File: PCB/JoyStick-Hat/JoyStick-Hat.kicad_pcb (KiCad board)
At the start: 4 copper layers, 65 x 120 mm, 114 parts, among them J1 20021121-00010C4LF, J10 Conn_02x06_Odd_Even, J14 Conn_01x03_Pin, J15 Conn_01x03_Pin, J2 BU2032SM-JJ-GTR, J3 Conn_02x05_Odd_Even, J4 Conn_02x04_Odd_Even, J5 8P8C_LED_Shielded, J6 1757242, J7 Raspberry_Pi_2_3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

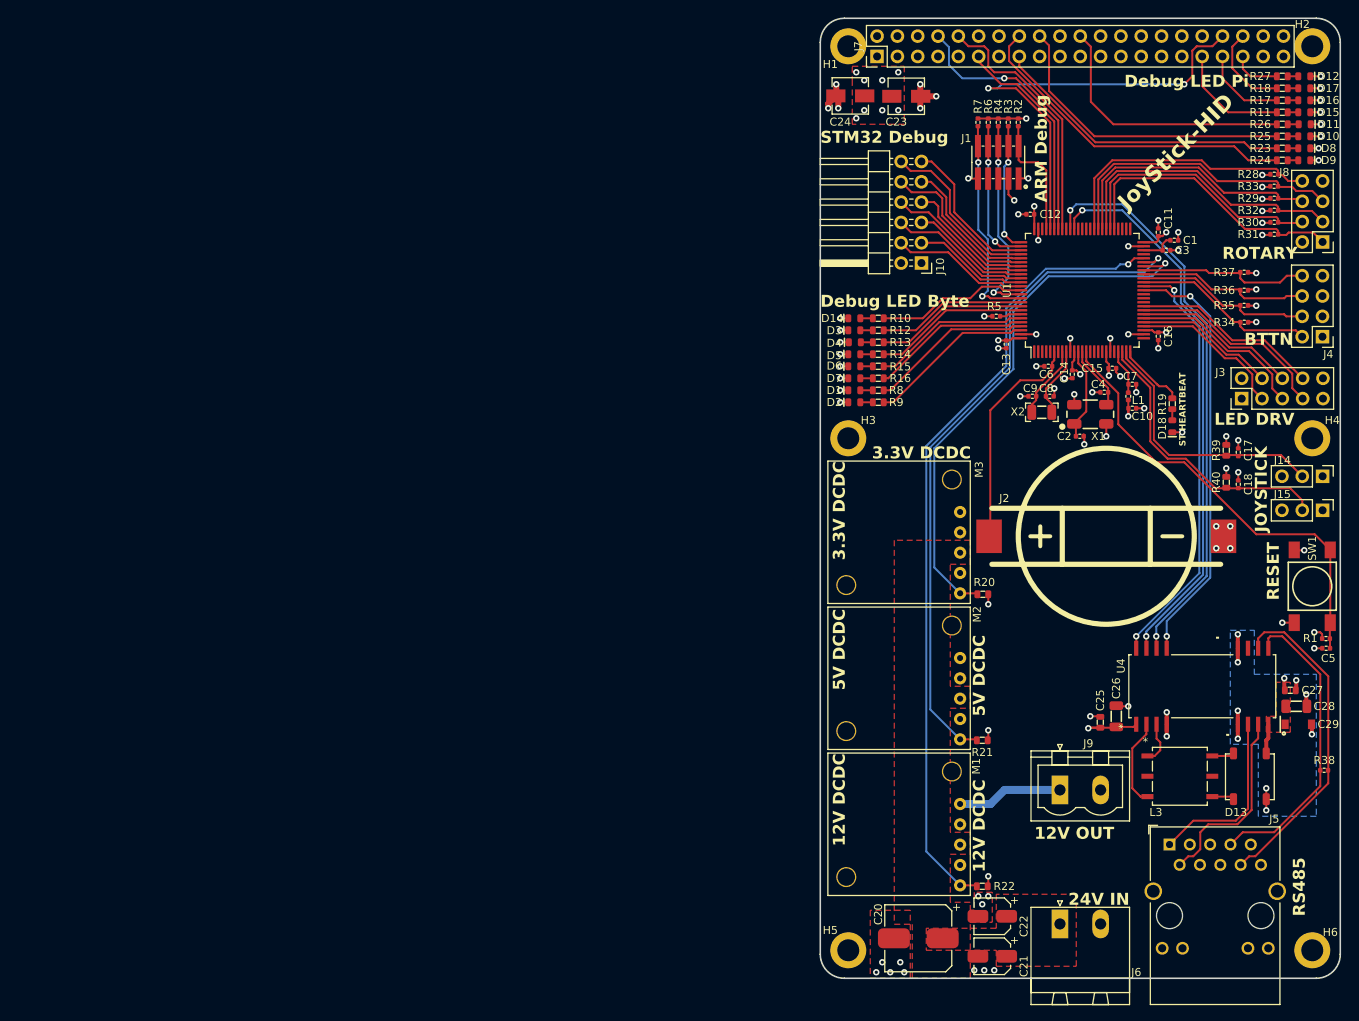
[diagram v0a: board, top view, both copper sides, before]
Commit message: RJ45
Replaced RJ45 connector, original one had magnetics, those are not needed for RS485 and would have caused problems. Hooked up coms LEDs on RJ45 connector to MCU for debugging and displaying coms activity.
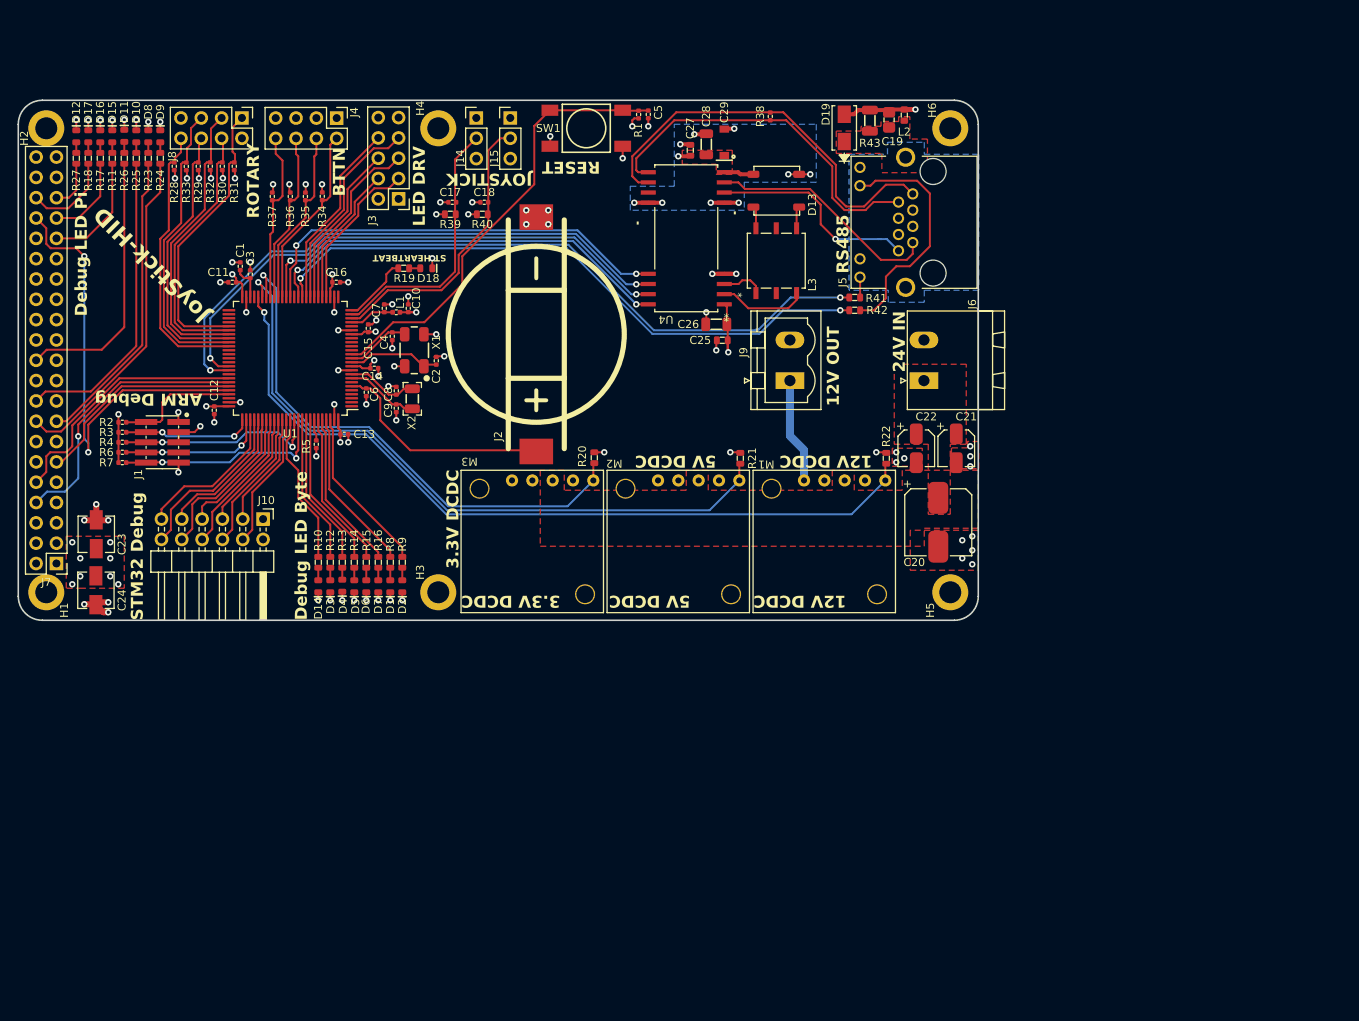
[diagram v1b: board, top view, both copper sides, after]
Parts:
- added C19: C0805C103KCRACAUTO, AVR-KiCAD-Lib-Capacitors:C0805, F.Cu at (208.6, 52.2)
- added D19: SMAJ30CA, AVR-KiCAD-Lib-Diodes:SMAJ30CA, F.Cu at (203.0, 53.2)
- added L2: MI0603K300R-10, AVR-KiCAD-Lib-Inductors:MI0603K300R-10, F.Cu at (210.5, 51.6)
- added R41: RC0603FR-07470RL, AVR-KiCAD-Lib-Resistors:R0603, F.Cu at (204.3, 74.4)
- added R42: RC0603FR-07470RL, AVR-KiCAD-Lib-Resistors:R0603, F.Cu at (204.3, 76.0)
- added R43: RC1206FR-071ML, AVR-KiCAD-Lib-Resistors:R1206, F.Cu at (206.2, 52.3)
- J5: value 8P8C_LED_Shielded -> RJHSE-5381; footprint AVR-KiCAD-Lib-Connectors:RJ45_Wuerth_7499111446_Horizontal -> AVR-KiCAD-Lib-Connectors:AMPHENOL_RJHSE-5381
- moved H2 158.6 mm to (103.2, 53.2), turned to 90 degrees
- moved D12 153.7 mm to (107.0, 54.2), turned to 90 degrees
- moved D17 152.1 mm to (108.5, 54.2), turned to 90 degrees
- moved R27 151.1 mm to (107.0, 57.0), turned to -90 degrees
- moved D16 150.6 mm to (110.0, 54.2), turned to 90 degrees
- moved R18 149.5 mm to (108.5, 57.0), turned to -90 degrees
- moved D15 149.0 mm to (111.5, 54.2), turned to 90 degrees
- moved R17 147.9 mm to (110.0, 57.0), turned to -90 degrees
- moved D11 147.6 mm to (113.0, 54.2), turned to 90 degrees
- moved R11 146.4 mm to (111.5, 57.0), turned to -90 degrees
- moved D10 146.0 mm to (114.5, 54.2), turned to 90 degrees
- moved R26 144.8 mm to (113.0, 57.0), turned to -90 degrees
- moved D8 144.5 mm to (116.0, 54.2), turned to 90 degrees
- moved R25 143.3 mm to (114.5, 57.0), turned to -90 degrees
- moved D9 143.0 mm to (117.5, 54.2), turned to 90 degrees
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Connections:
- J5 pad 1: Net-(U4-Z) -> Net-(U4-A)
- J5 pad 10: unconnected-(J5-Pad10) -> Net-(J5-Pad10)
- J5 pad 11: unconnected-(J5-Pad11) -> GND
- J5 pad 12: unconnected-(J5-Pad12) -> Net-(J5-Pad12)
- J5 pad 2: Net-(U4-Y) -> Net-(U4-B)
- J5 pad 7: Net-(U4-B) -> Net-(U4-Y)
- J5 pad 8: Net-(U4-A) -> Net-(U4-Z)
- J5 pad 9: unconnected-(J5-Pad9) -> GND
- U1 pad 35: unconnected-(U1-PB0-Pad35) -> /RS485 To Motor Controller Interface/RS485_RX_LED
- U1 pad 36: unconnected-(U1-PB1-Pad36) -> /RS485 To Motor Controller Interface/RS485_TX_LED
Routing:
- net /RS485 To Motor Controller Interface/RS485_TX_LED: track 0.00 -> 80.1 mm, vias 0 -> 2
- net /RS485 To Motor Controller Interface/RS485_RX_LED: track 0.00 -> 78.2 mm, vias 0 -> 2
- net Net-(J5-Pad10): track 0.00 -> 29.9 mm
- net GND: track 431.6 -> 442.4 mm, vias 73 -> 74
- net Net-(U4-A): track 41.1 -> 50.9 mm
- net Net-(U4-B): track 38.1 -> 45.2 mm
- net Net-(U4-Y): track 24.1 -> 29.3 mm
- net Net-(U4-Z): track 22.2 -> 26.2 mm, vias 0 -> 1
- net Net-(J5-Pad12): track 0.00 -> 2.55 mm
- added copper zone on B.Cu, net /RS485 To Motor Controller Interface/RJ45_SHIELD
- added copper zone on F.Cu, net /RS485 To Motor Controller Interface/RJ45_SHIELD
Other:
- board size 65 x 120 mm -> 120 x 65 mm
- board text added: "https://github.com/Accessibilita"

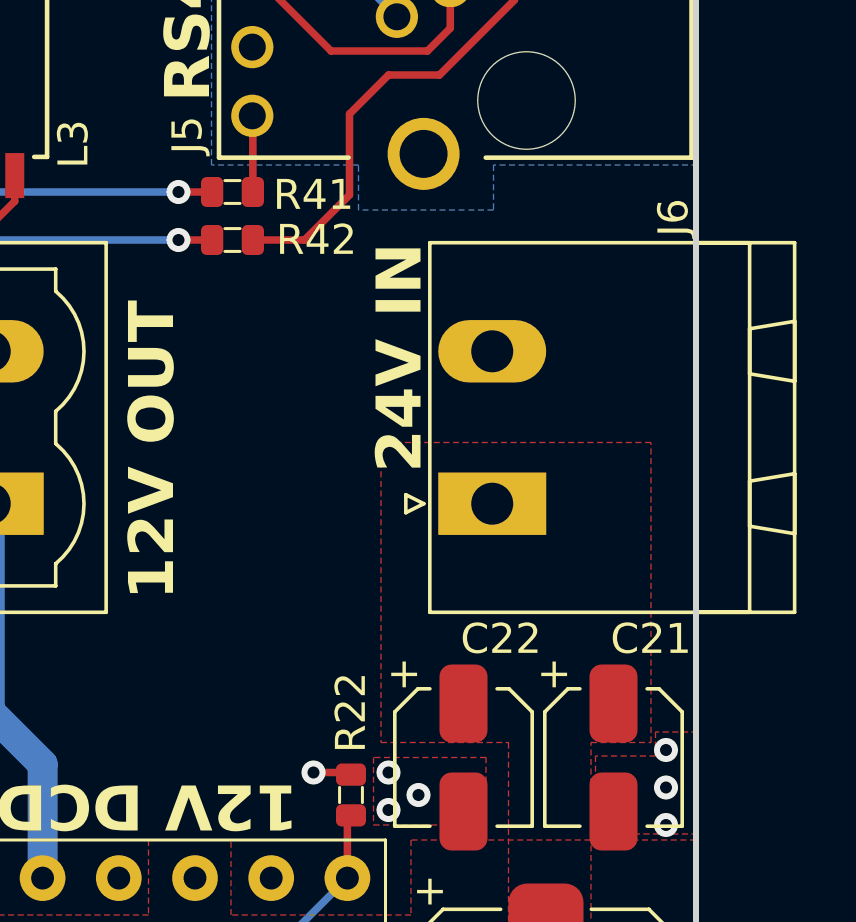
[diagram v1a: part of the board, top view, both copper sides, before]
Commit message: Power Input Moved
Power input connector moved to be flush with board!
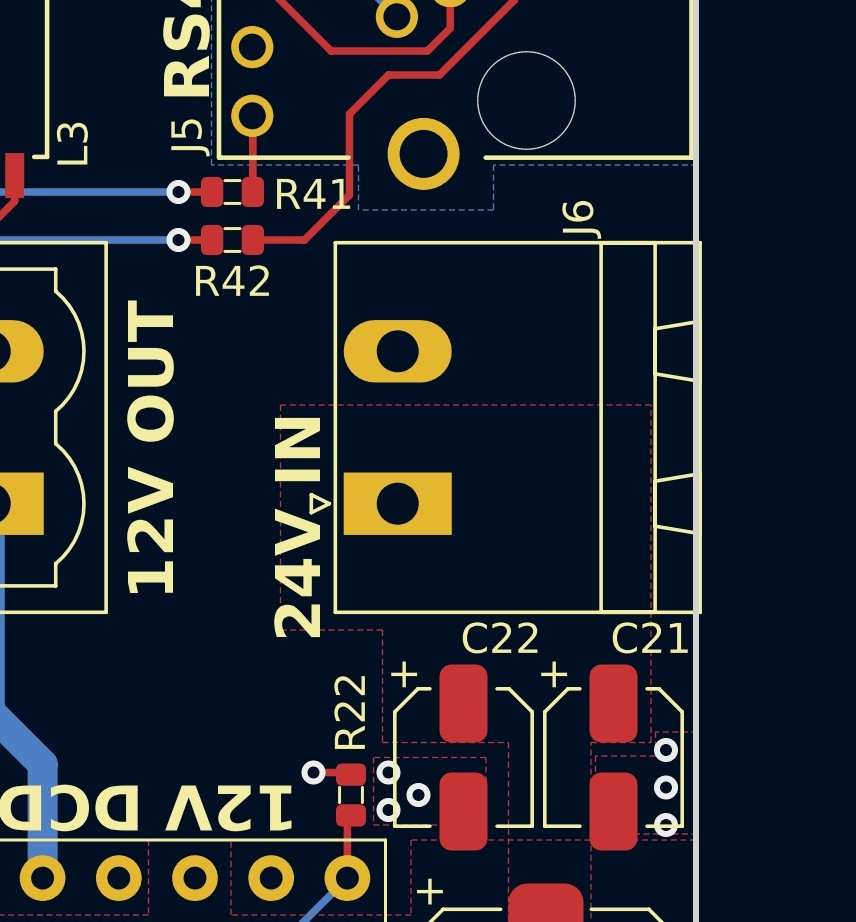
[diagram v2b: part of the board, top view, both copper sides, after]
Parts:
- moved J6 3.15 mm to (209.8, 84.8)
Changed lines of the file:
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@@
 		(at 204.3 76 180)
 		(property "Reference" "R42"
-			(at -2.8 0 180)
+			(at 0 -1.4 180)
 			(layer "F.SilkS")
 			(effects
@@
 	(footprint "AVR-KiCAD-Lib-Connectors:PhoenixContact_MSTBA-G_02x5.08mm_Angled"
 		(layer "F.Cu")
-		(at 212.9575 84.79 90)
+		(at 209.8075 84.79 90)
 		(descr "Generic Phoenix Contact connector footprint for series: MSTBA-G; number of pins: 02; pin pitch: 5.08mm; Angled || order number: 1757242 12A || order number: 1923869 16A (HC)")
 		(tags "phoenix_contact connector MSTBA_01x02_G_5.08mm")
@@
 	)
 	(gr_text "24V IN"
-		(at 210.75 83.75 90)
+		(at 207.4 89.4 90)
 		(layer "F.SilkS")
 		(effects
@@
 		(polygon
 			(pts
-				(xy 209.25 82.75) (xy 209.25 92.75) (xy 213.5 92.75) (xy 213.5 101.5) (xy 216.25 101.5) (xy 216.25 92.75)
-				(xy 218.25 92.75) (xy 218.25 82.75)
+				(xy 205.9 81.5) (xy 205.9 89) (xy 209.3 89) (xy 209.3 92.75) (xy 213.5 92.75) (xy 213.5 101.5) (xy 216.25 101.5)
+				(xy 216.25 92.75) (xy 218.25 92.75) (xy 218.25 81.5)
 			)
 		)

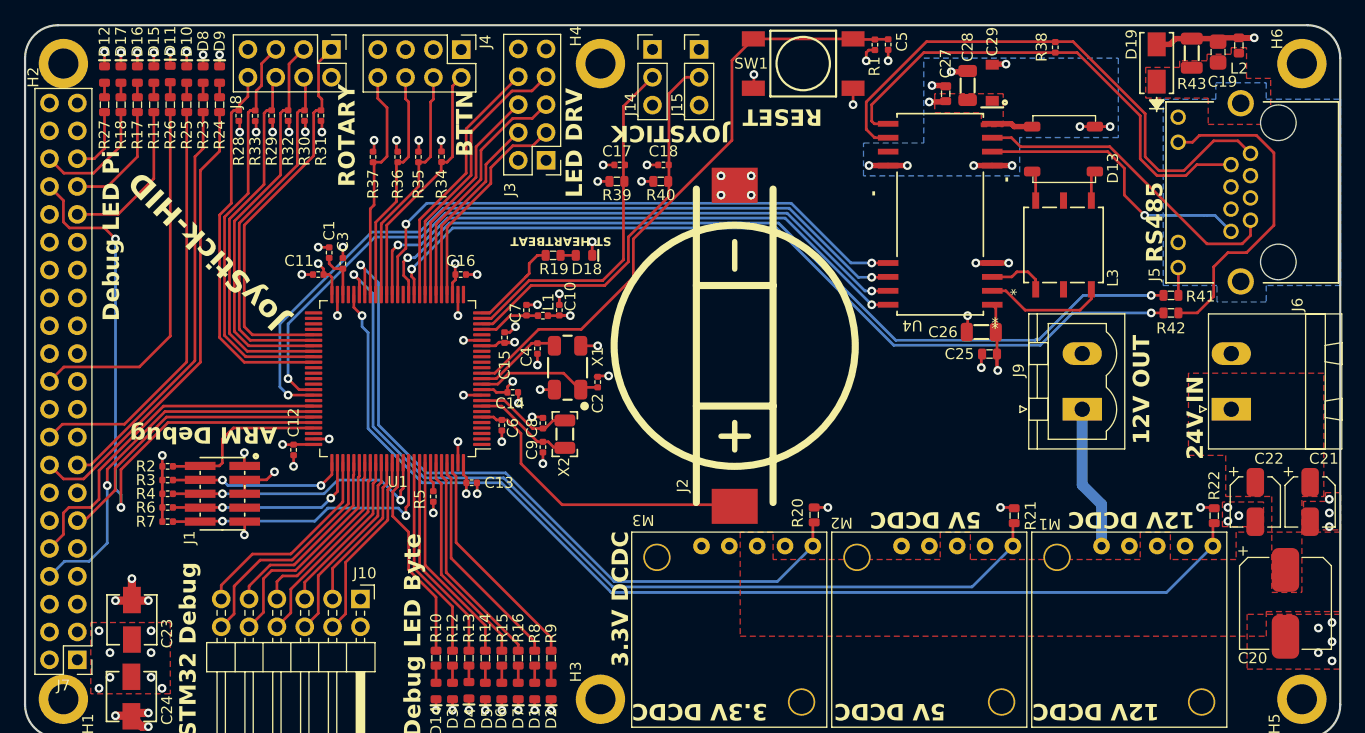
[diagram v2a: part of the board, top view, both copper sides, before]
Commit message: Board Tweaks
Copper pour specifications adjusted and repoured. DRC errors are caused by silkscreen , this happened when updating from KiCAD 7 to 8, still investigating it.
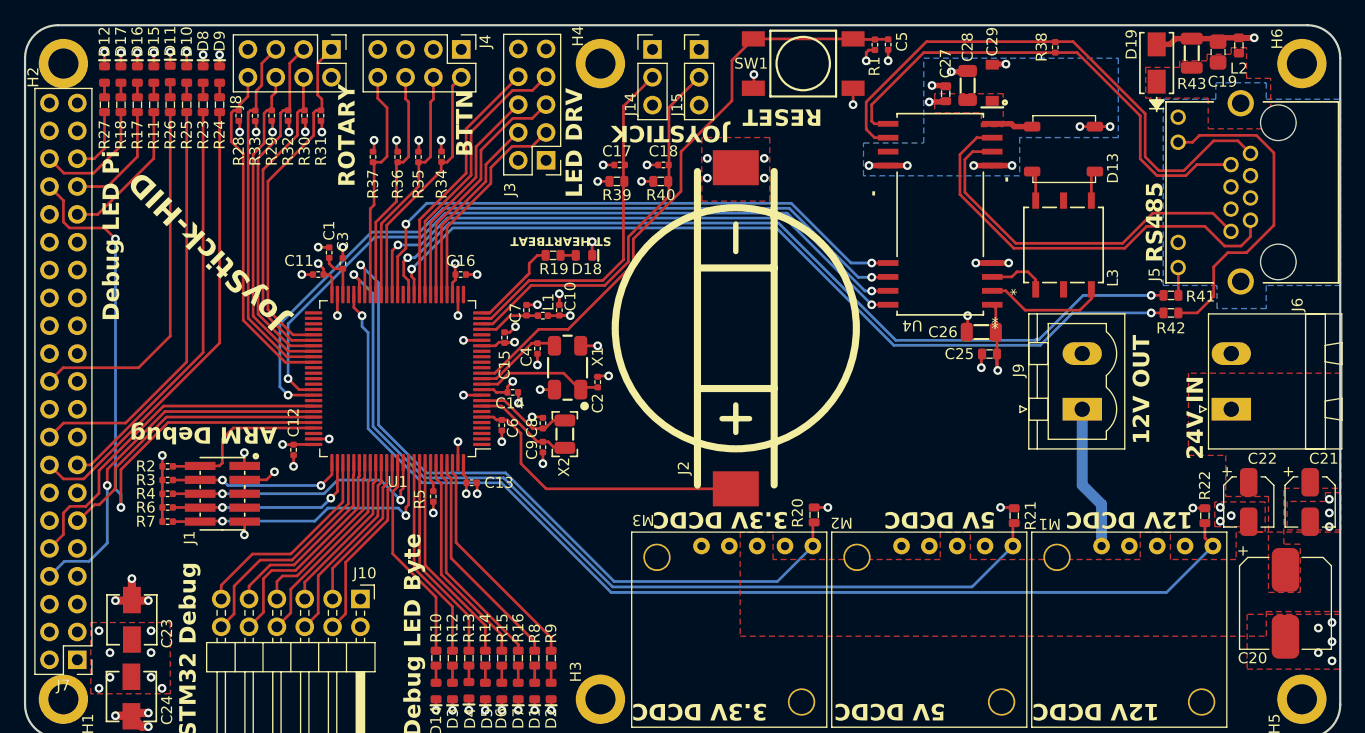
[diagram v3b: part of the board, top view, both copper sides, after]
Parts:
- moved J2 1.60 mm to (164.6, 77.4)
- moved R22 0.85 mm to (207.4, 94.5)
- moved C22 0.60 mm to (211.4, 93.2)
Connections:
- net Net-(U4-A) renamed /RS485 To Motor Controller Interface/A_RS485
- net Net-(U4-B) renamed /RS485 To Motor Controller Interface/B_RS485
- net Net-(U4-Y) renamed /RS485 To Motor Controller Interface/Y_RS485
- net Net-(U4-Z) renamed /RS485 To Motor Controller Interface/Z_RS485
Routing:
- net /RS485 To Motor Controller Interface/Y_RS485: track 29.3 -> 39.2 mm
- net /RS485 To Motor Controller Interface/Z_RS485: track 26.2 -> 33.8 mm, vias 1 -> 0
- net /JoyStick Interface/ROTARY2_POLE2: track 33.8 -> 29.7 mm
- net /JoyStick Interface/ROTARY1_POLE3: track 37.3 -> 33.3 mm
- net /JoyStick Interface/ROTARY1_POLE2: track 36.4 -> 32.5 mm
- net /JoyStick Interface/ROTARY1_POLE1: track 35.8 -> 31.9 mm
- net /JoyStick Interface/ROTARY2_POLE3: track 33.1 -> 29.3 mm
- net /JoyStick Interface/ROTARY2_POLE1: track 34.6 -> 31.6 mm
- net Net-(J7-PWM1/GPIO13): track 14.4 -> 13.3 mm
- net /JoyStick Interface/JOYSTICK_Y: track 36.0 -> 35.2 mm
- net /STM32F446RET6-MCU/NRST: track 56.1 -> 55.4 mm
